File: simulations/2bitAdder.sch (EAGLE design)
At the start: 34 parts

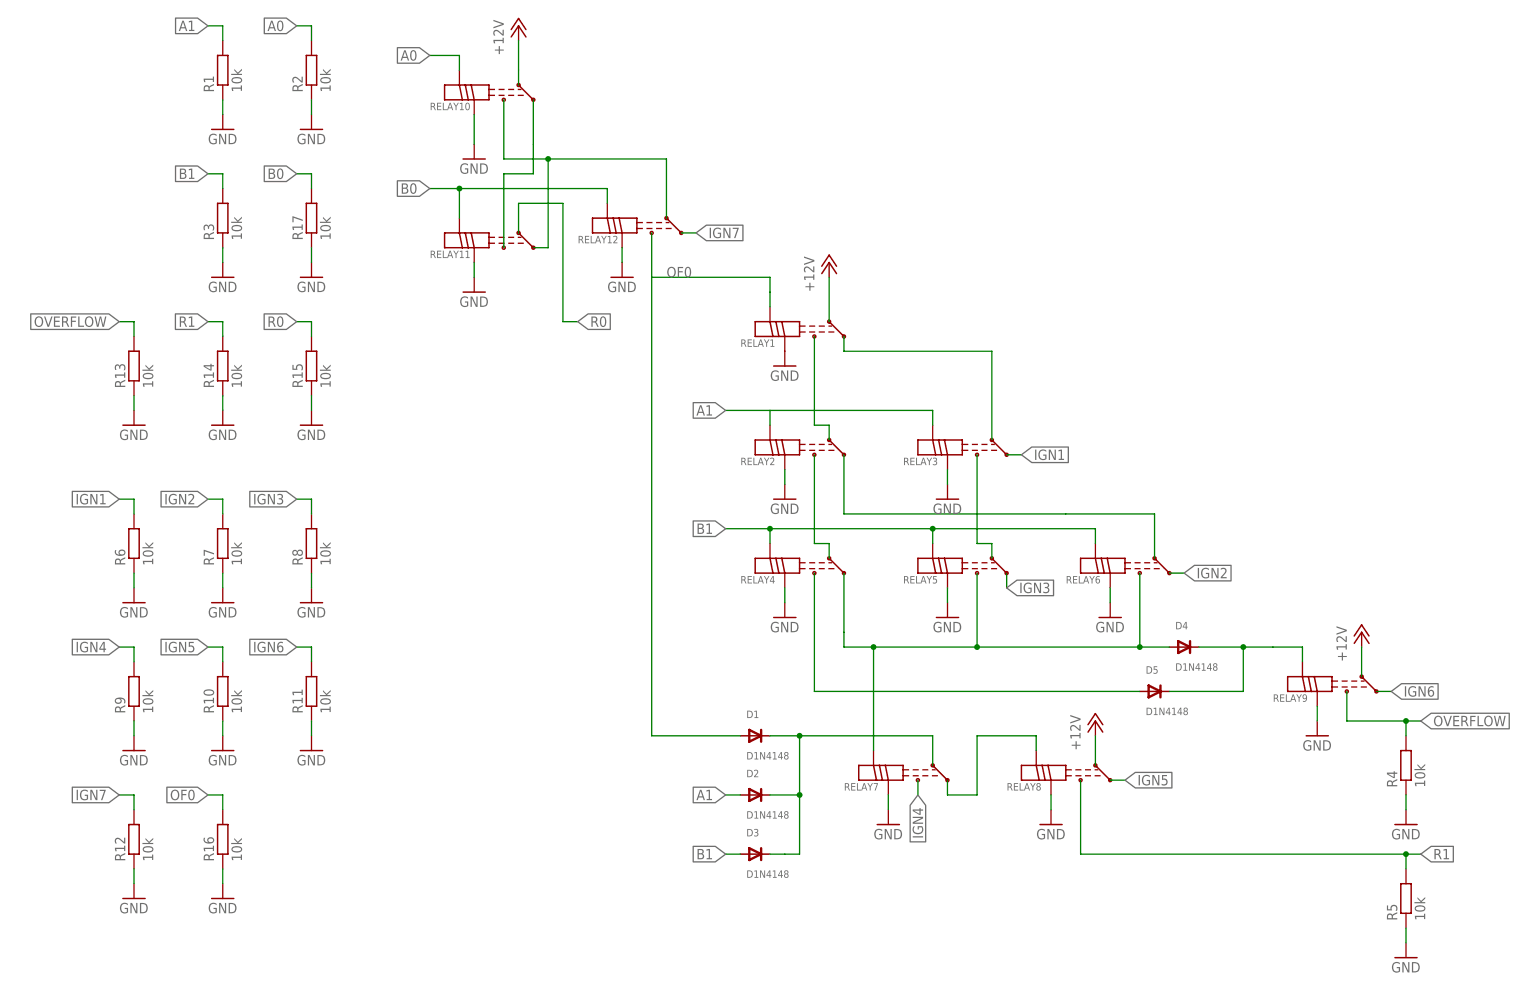
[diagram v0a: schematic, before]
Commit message: Refactoring 2 bit adder
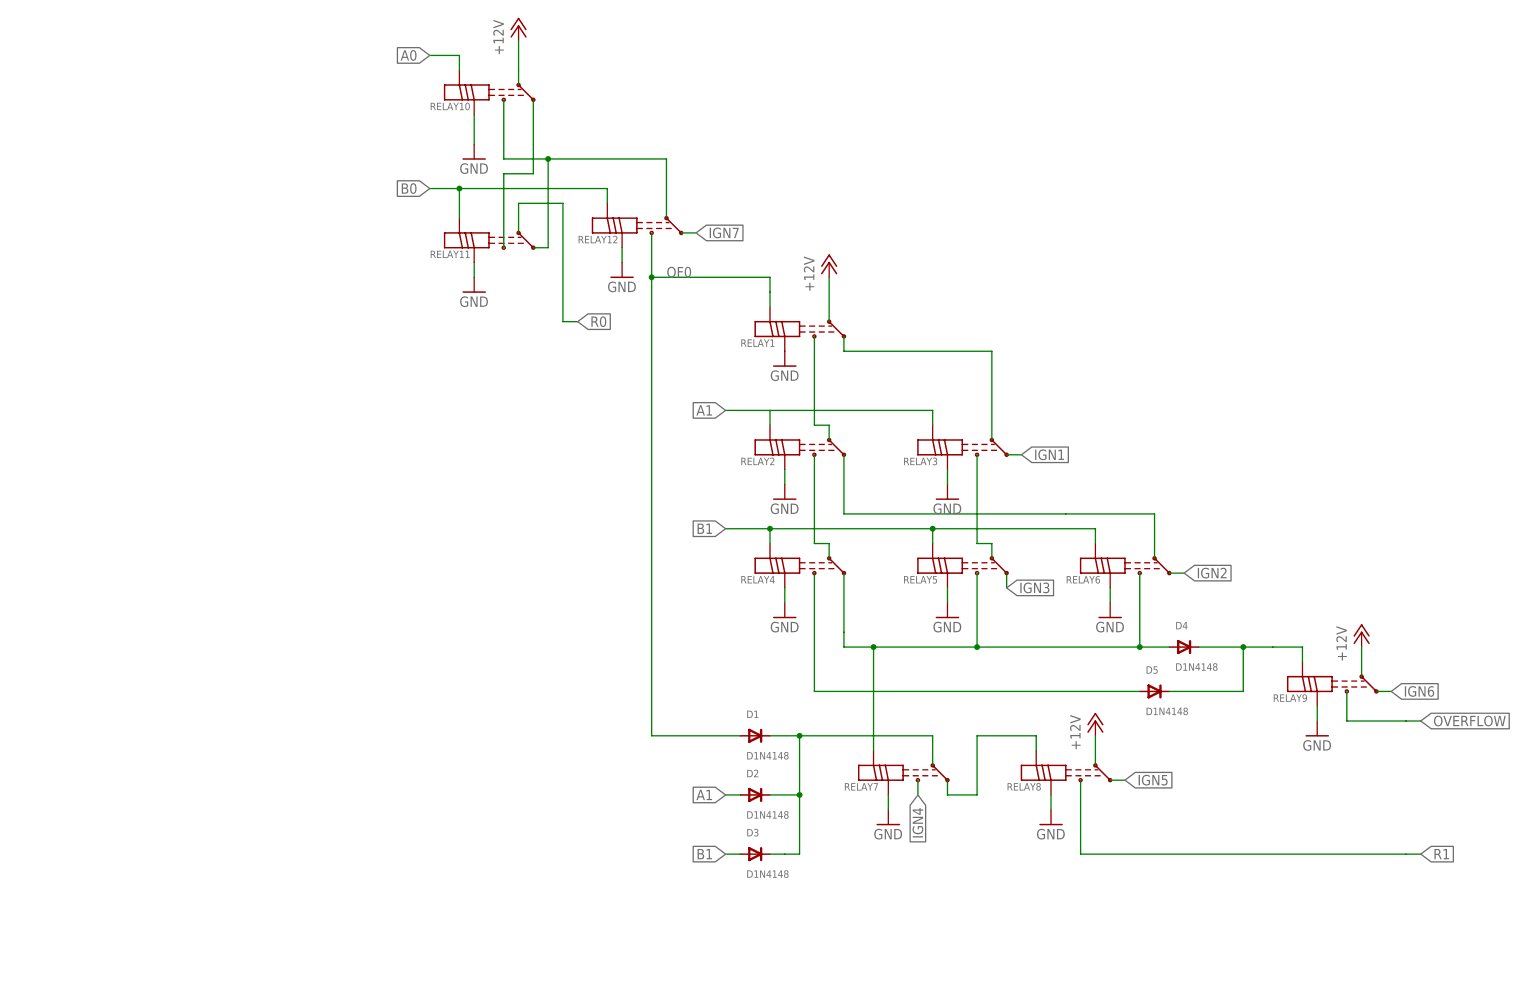
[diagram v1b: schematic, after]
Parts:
- removed R1, R10, R11, R12, R13, R14, R15, R16, R17, R2, R3, R4, R5, R6, R7, R8, R9: 10k, p.peter-scoville.tests:R-EU_R0603
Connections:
- net A0: no longer R2.2
- net A1: no longer R1.2
- net B0: no longer R17.2
- net B1: no longer R3.2
- net GND: no longer R1.1, R10.1, R11.1, R12.1, R13.1, R14.1, R15.1, R16.1, R17.1, R2.1, R3.1, R4.1, R5.1, R6.1, R7.1, R8.1, R9.1
- net IGN1: no longer R6.2
- net IGN2: no longer R7.2
- net IGN3: no longer R8.2
- net IGN4: no longer R9.2
- net IGN5: no longer R10.2
- net IGN6: no longer R11.2
- net IGN7: no longer R12.2
- net OF0: no longer R16.2
- net OVERFLOW: no longer R13.2, R4.2
- net R0: no longer R15.2
- net R1: no longer R14.2, R5.2
